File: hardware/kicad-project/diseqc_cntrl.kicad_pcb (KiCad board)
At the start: 4 copper layers, 90 x 100 mm, 131 parts, among them IC1 TPS560200DBVR, IC2 STM32F407VGT6, IC3 USBLC6-2P6, IC4 FM24CL16B-GTR, IC5 LNBH26PQR, IC6 W5500, J1 Barrel Jack, J3 Conn_01x04_Pin, J4 USB4110-GF-A, J5 USB4110-GF-A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

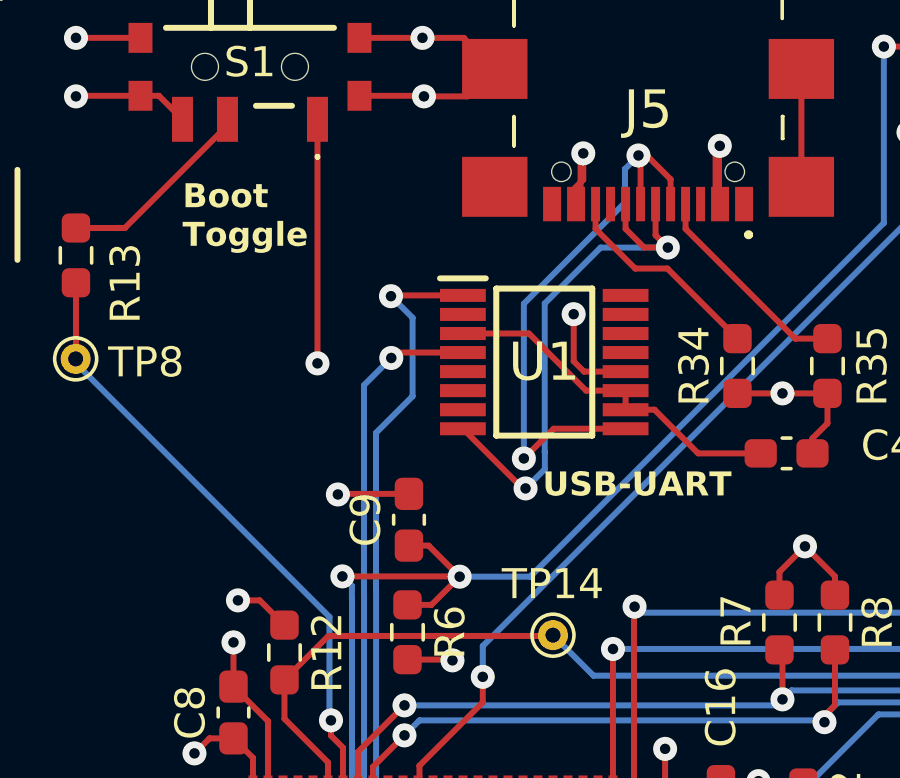
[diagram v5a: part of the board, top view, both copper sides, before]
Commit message: Added FT230X decoupling (C44)
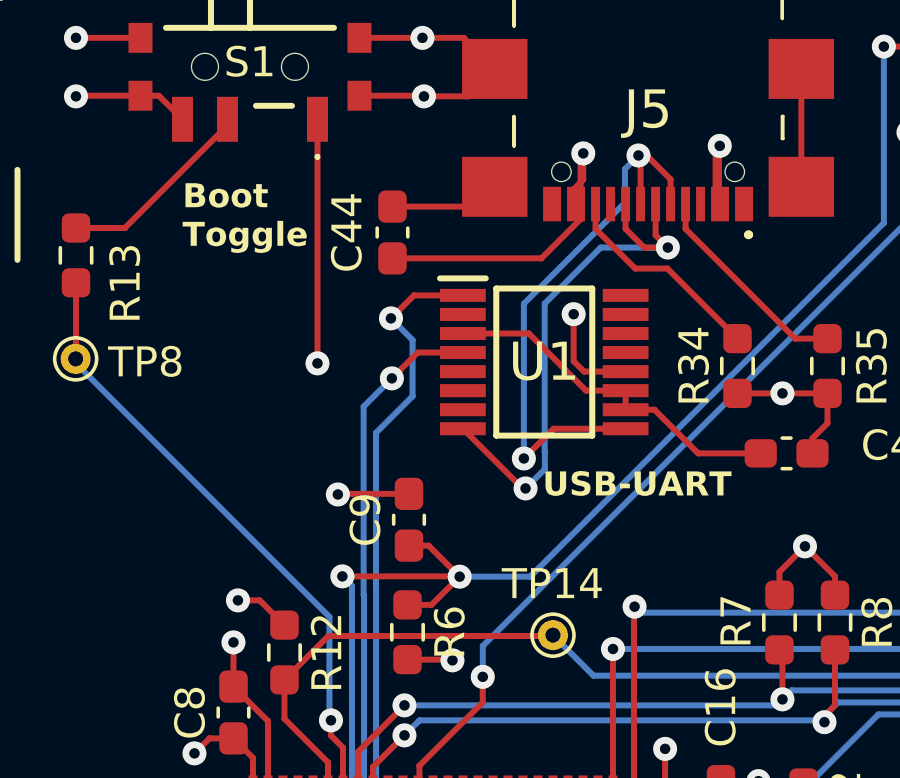
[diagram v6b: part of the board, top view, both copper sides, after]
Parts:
- added C44: 10n, Capacitor_SMD:C_0603_1608Metric_Pad1.08x0.95mm_HandSolder, F.Cu at (100.0, 59.6)
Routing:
- net /MCU/USB-UART/FT230_VCC: track 11.0 -> 18.4 mm
- net GND: track 258.3 -> 262.0 mm

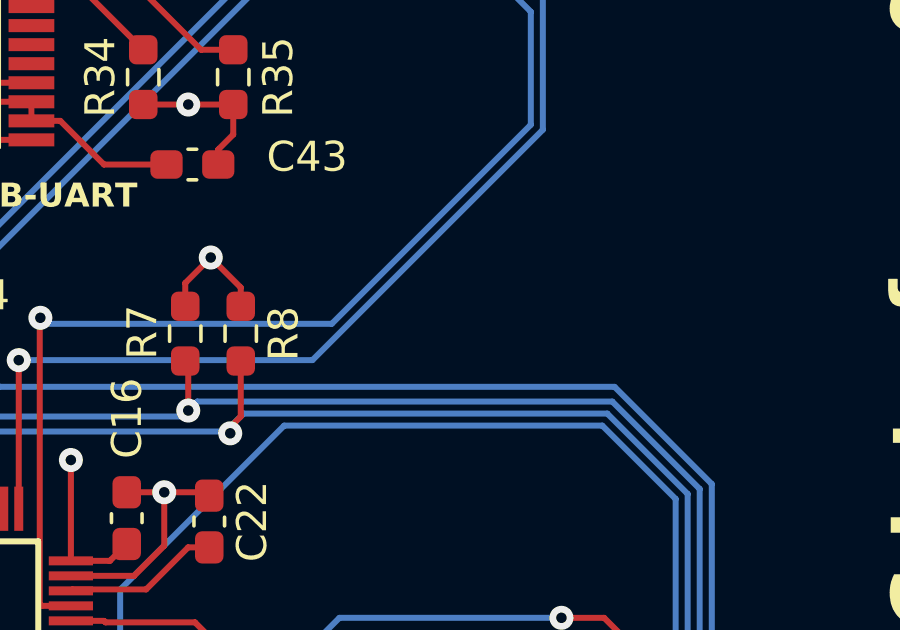
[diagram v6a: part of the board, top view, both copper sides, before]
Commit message: Added test points for I2C1
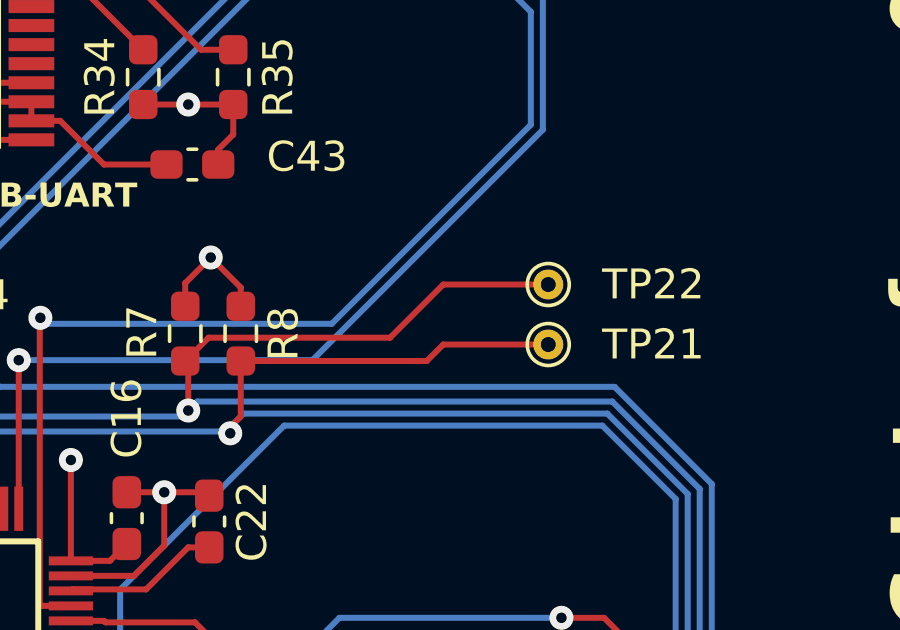
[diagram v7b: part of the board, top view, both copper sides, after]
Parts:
- added TP21: TP_I2C1_SCL, TestPoint:TestPoint_THTPad_D1.0mm_Drill0.5mm, F.Cu at (125.0, 73.0)
- added TP22: TP_I2C1_SDA, TestPoint:TestPoint_THTPad_D1.0mm_Drill0.5mm, F.Cu at (125.0, 71.0)
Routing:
- net /MCU/I2C1_SDA: track 124.8 -> 138.0 mm
- net /MCU/I2C1_SCL: track 121.8 -> 132.3 mm
